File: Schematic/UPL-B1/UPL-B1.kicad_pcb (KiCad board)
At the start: 2 copper layers, 154.7 x 128.7 mm, 0 parts

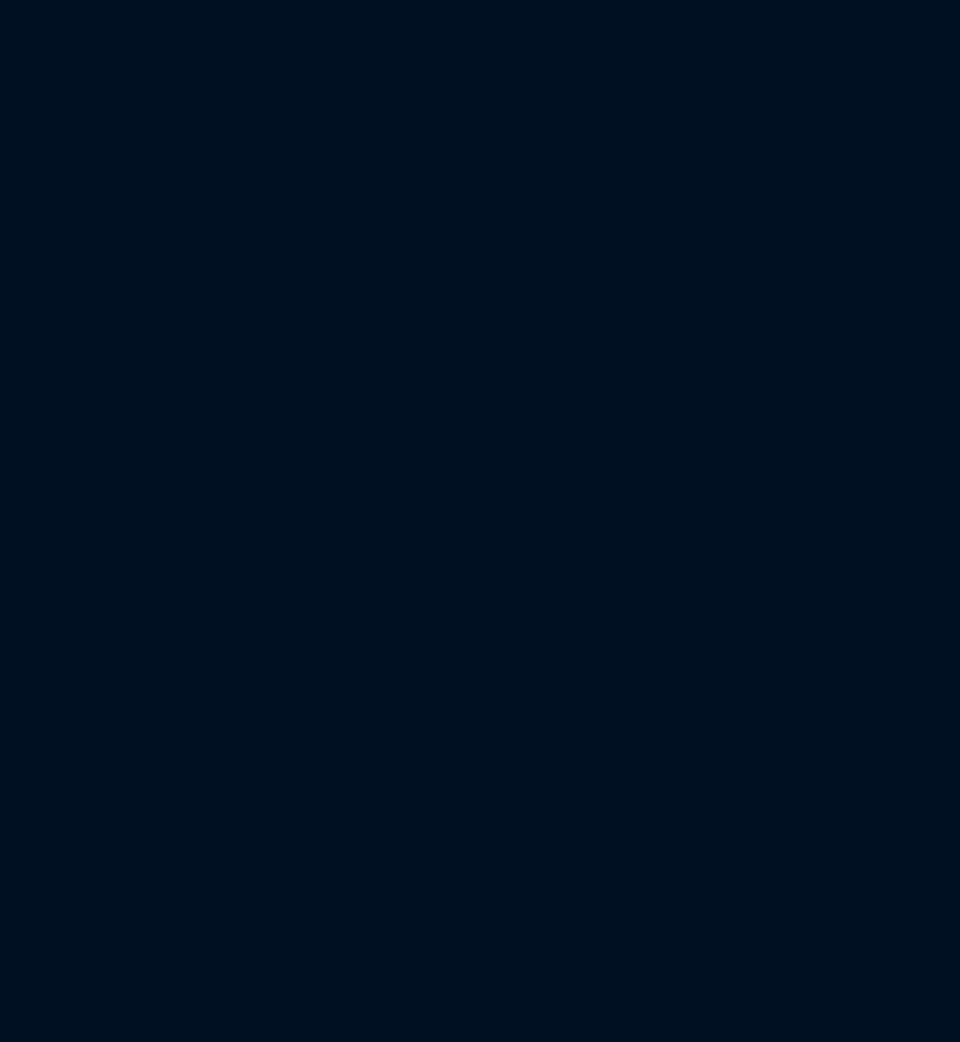
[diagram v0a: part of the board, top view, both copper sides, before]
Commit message: Minor fixups for layout.
Reannotate, deduplicate N53B. Add some hierachical pins. First
preparations for layout
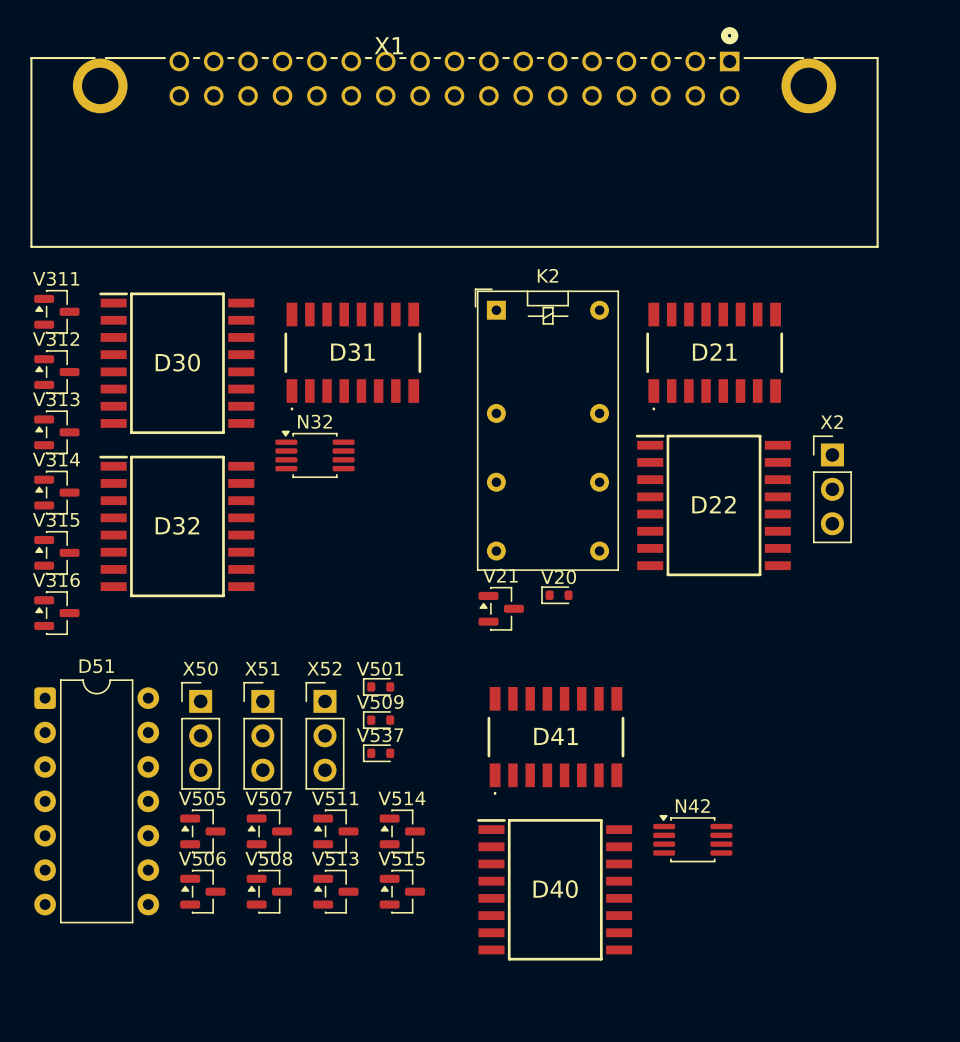
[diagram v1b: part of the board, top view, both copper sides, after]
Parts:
- added D21: 74HCT4094D,118, UPL_B1:74HCT4094D118, F.Cu at (25.4, 45.4)
- added D22: DAC8143FSZ, UPL_B1:SOIC127P1032X265-16N, F.Cu at (25.4, 56.6)
- added D30: DAC8143FSZ, UPL_B1:SOIC127P1032X265-16N, F.Cu at (-14.3, 46.1)
- added D31: 74HCT4094D,118, UPL_B1:74HCT4094D118, F.Cu at (-1.31, 45.4)
- added D32: DAC8143FSZ, UPL_B1:SOIC127P1032X265-16N, F.Cu at (-14.3, 58.2)
- added D40: DAC8143FSZ, UPL_B1:SOIC127P1032X265-16N, F.Cu at (13.6, 85.0)
- added D41: 74HCT4094D,118, UPL_B1:74HCT4094D118, F.Cu at (13.7, 73.7)
- added D51: MC1595, Package_DIP:DIP-14_W7.62mm, F.Cu at (-24.0, 70.9)
- added K2: G5V-2_Split, Relay_THT:Relay_DPDT_Omron_G5V-2, F.Cu at (9.29, 42.2)
- added N32: HA7-5221, Package_SO:MSOP-8_3x3mm_P0.65mm, F.Cu at (-4.10, 52.9)
- added N42: HA7-5221, Package_SO:MSOP-8_3x3mm_P0.65mm, F.Cu at (23.8, 81.3)
- added V20: BAS32, Diode_SMD:D_SOD-523, F.Cu at (13.9, 63.3)
- added V21: BC850B, Package_TO_SOT_SMD:SOT-23, F.Cu at (9.65, 64.3)
- added V311: BAV70, Package_TO_SOT_SMD:SOT-23, F.Cu at (-23.2, 42.3)
- added V312: BAV70, Package_TO_SOT_SMD:SOT-23, F.Cu at (-23.2, 46.8)
- added V313: BAV70, Package_TO_SOT_SMD:SOT-23, F.Cu at (-23.2, 51.2)
- added V314: BAV99, Package_TO_SOT_SMD:SOT-23, F.Cu at (-23.2, 55.7)
- added V315: BC860, Package_TO_SOT_SMD:SOT-23, F.Cu at (-23.2, 60.1)
- added V316: BC860, Package_TO_SOT_SMD:SOT-23, F.Cu at (-23.2, 64.6)
- added V501: BAS32, Diode_SMD:D_SOD-523, F.Cu at (0.75, 70.0)
- added V505: BC850B, Package_TO_SOT_SMD:SOT-23, F.Cu at (-12.4, 80.7)
- added V506: BC850B, Package_TO_SOT_SMD:SOT-23, F.Cu at (-12.4, 85.2)
- added V507: BC860B, Package_TO_SOT_SMD:SOT-23, F.Cu at (-7.47, 80.7)
- added V508: BC860B, Package_TO_SOT_SMD:SOT-23, F.Cu at (-7.47, 85.2)
- added V509: BAS32, Diode_SMD:D_SOD-523, F.Cu at (0.75, 72.5)
- added V511: BAV70, Package_TO_SOT_SMD:SOT-23, F.Cu at (-2.56, 80.7)
- added V513: BAV99, Package_TO_SOT_SMD:SOT-23, F.Cu at (-2.56, 85.2)
- added V514: BAV99, Package_TO_SOT_SMD:SOT-23, F.Cu at (2.35, 80.7)
- added V515: BAV99, Package_TO_SOT_SMD:SOT-23, F.Cu at (2.35, 85.2)
- added V537: BAS32, Diode_SMD:D_SOD-523, F.Cu at (0.75, 74.9)
- added X1: 5102159-8, UPL_B1:TYCO_5102159-8, F.Cu at (-14.1, 26.4)
- added X2: Conn_01x03_Pin_Bridge, Connector_PinHeader_2.54mm:PinHeader_1x03_P2.54mm_Vertical, F.Cu at (34.1, 52.9)
- added X50: Conn_01x03_Pin_Bridge, Connector_PinHeader_2.54mm:PinHeader_1x03_P2.54mm_Vertical, F.Cu at (-12.5, 71.1)
- added X51: Conn_01x03_Pin_Bridge, Connector_PinHeader_2.54mm:PinHeader_1x03_P2.54mm_Vertical, F.Cu at (-7.95, 71.1)
- added X52: Conn_01x03_Pin_Bridge, Connector_PinHeader_2.54mm:PinHeader_1x03_P2.54mm_Vertical, F.Cu at (-3.36, 71.1)

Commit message: updated DXF files for PCB
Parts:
- moved X1 123.3 mm to (36.6, 138.7)
- moved D21 45.9 mm to (-20.5, 46.8)
- moved D22 45.9 mm to (-20.5, 58.0)
- moved D30 45.9 mm to (-60.2, 47.5)
- moved D31 45.9 mm to (-47.2, 46.8)
- moved D32 45.9 mm to (-60.2, 59.6)
- moved D40 45.9 mm to (-32.3, 86.4)
- moved D41 45.9 mm to (-32.2, 75.1)
- moved K2 45.9 mm to (-36.6, 43.6)
- moved N32 45.9 mm to (-50.0, 54.3)
- moved N42 45.9 mm to (-22.1, 82.7)
- moved V20 45.9 mm to (-32.0, 64.7)
- moved V21 45.9 mm to (-36.3, 65.7)
- moved V311 45.9 mm to (-69.1, 43.7)
- moved V312 45.9 mm to (-69.1, 48.2)
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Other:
- board size 154.7 x 128.7 mm -> 155 x 130 mm
- board text added: "Origin for Graphics Import X180,Y20 Rotate if needed to have notch at bottom"

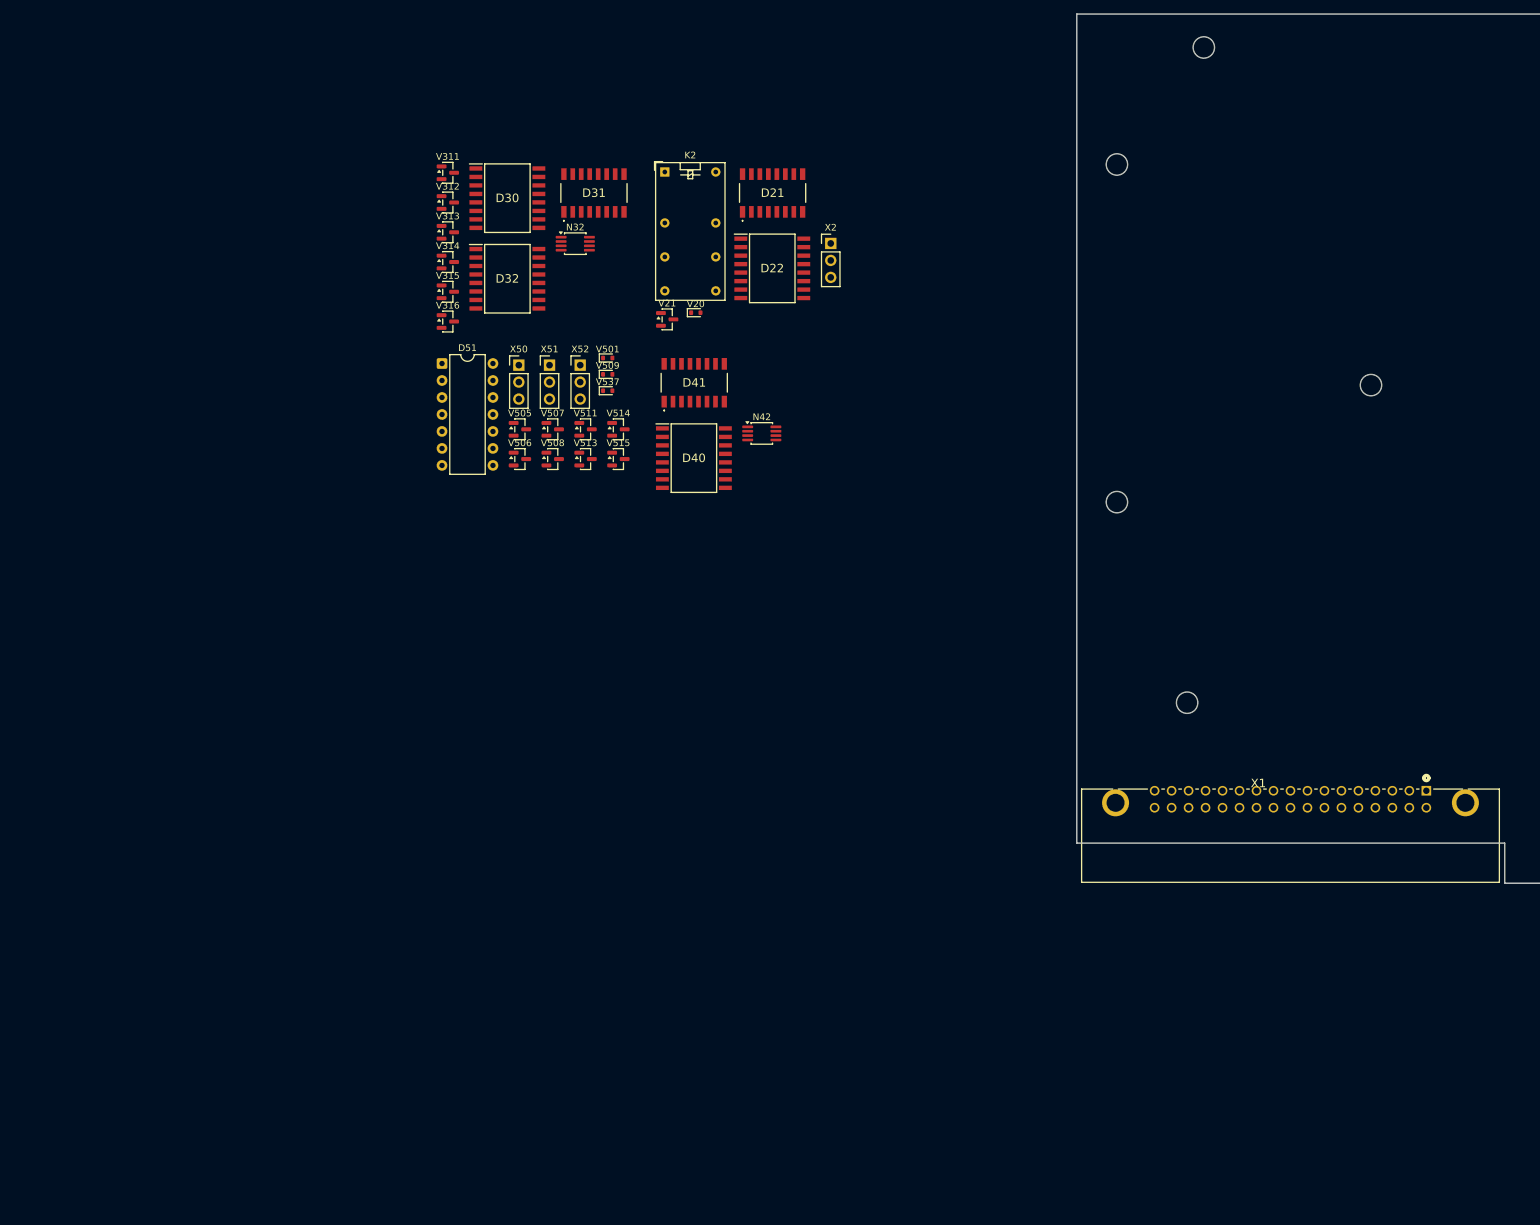
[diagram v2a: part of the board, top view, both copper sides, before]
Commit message: added majority of footprints
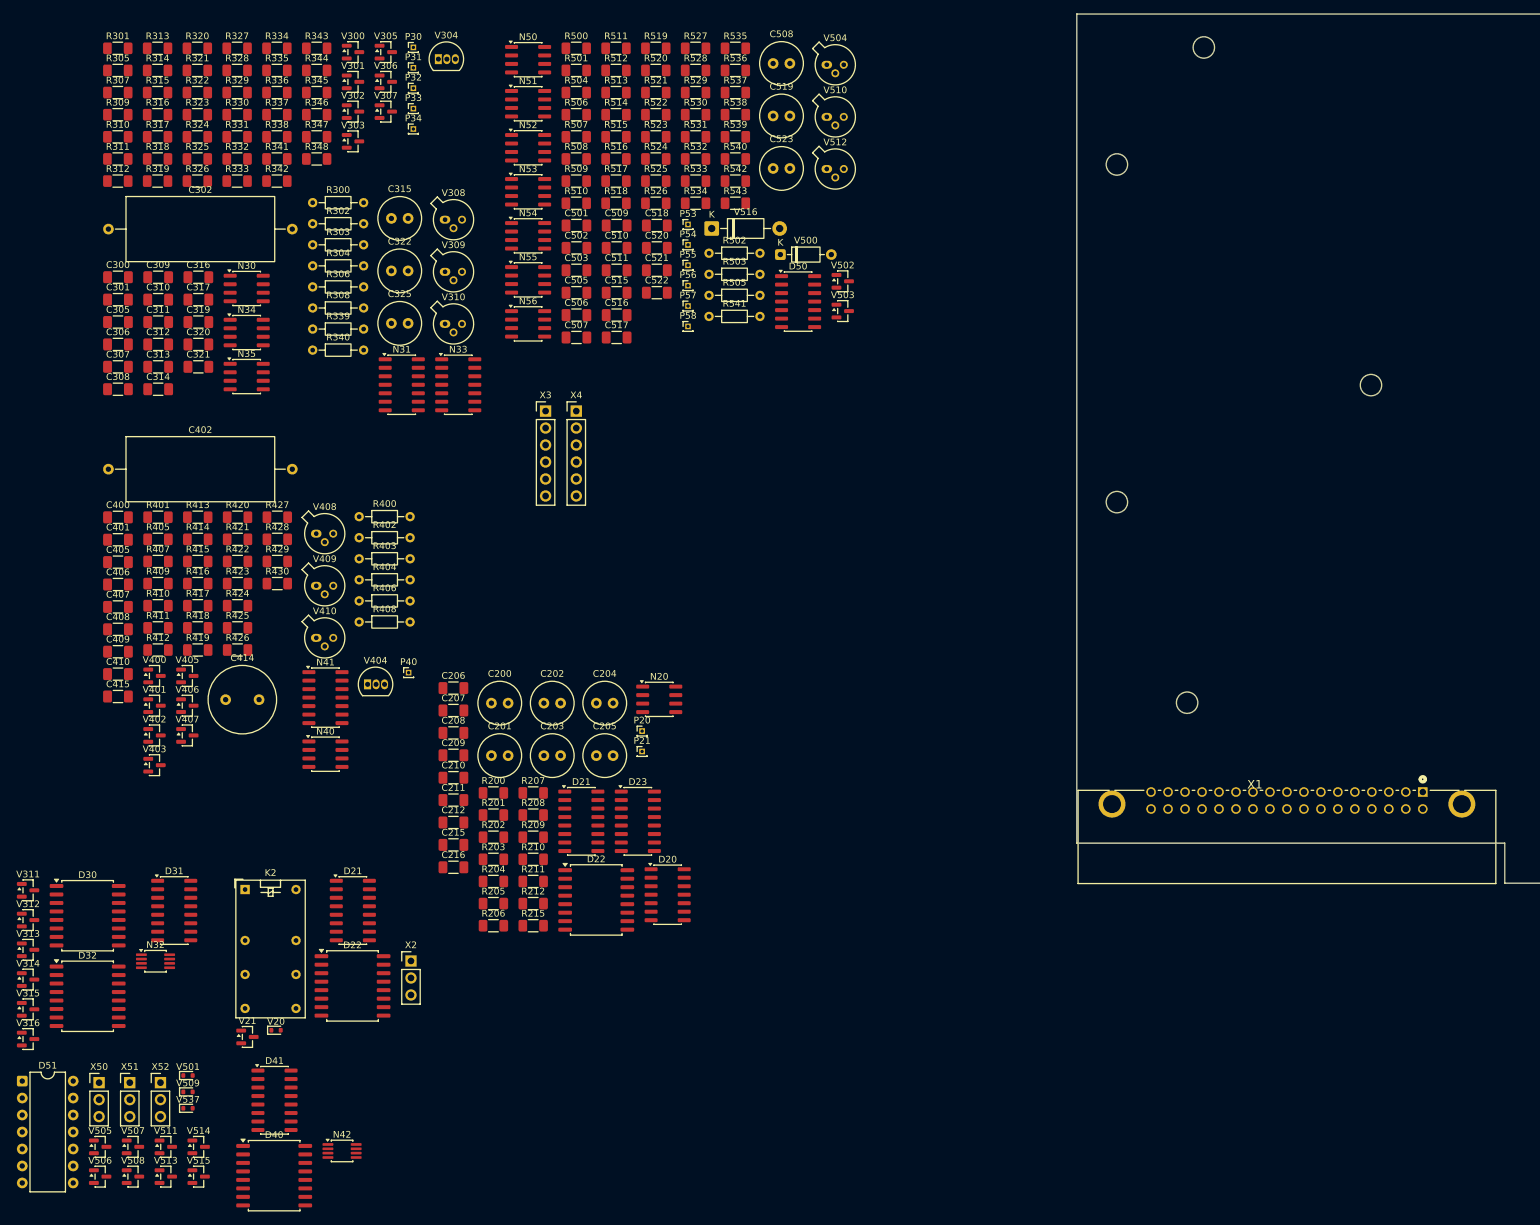
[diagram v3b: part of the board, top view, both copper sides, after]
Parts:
- added C200: 100uF 25V, Capacitor_THT:C_Radial_D6.3mm_H11.0mm_P2.50mm, F.Cu at (-62.6, 123.1)
- added C201: 100uF 25V, Capacitor_THT:C_Radial_D6.3mm_H11.0mm_P2.50mm, F.Cu at (-62.6, 130.9)
- added C202: 100uF 25V, Capacitor_THT:C_Radial_D6.3mm_H11.0mm_P2.50mm, F.Cu at (-54.7, 123.1)
- added C203: 100uF 25V, Capacitor_THT:C_Radial_D6.3mm_H11.0mm_P2.50mm, F.Cu at (-54.7, 130.9)
- added C204: 100uF 25V, Capacitor_THT:C_Radial_D6.3mm_H11.0mm_P2.50mm, F.Cu at (-46.9, 123.1)
- added C205: 100uF 25V, Capacitor_THT:C_Radial_D6.3mm_H11.0mm_P2.50mm, F.Cu at (-46.9, 130.9)
- added C206: 100nF, Capacitor_SMD:C_1206_3216Metric_Pad1.33x1.80mm_HandSolder, F.Cu at (-68.2, 120.8)
- added C207: 100nF, Capacitor_SMD:C_1206_3216Metric_Pad1.33x1.80mm_HandSolder, F.Cu at (-68.2, 124.2)
- added C208: 100nF, Capacitor_SMD:C_1206_3216Metric_Pad1.33x1.80mm_HandSolder, F.Cu at (-68.2, 127.5)
- added C209: 100nF, Capacitor_SMD:C_1206_3216Metric_Pad1.33x1.80mm_HandSolder, F.Cu at (-68.2, 130.9)
- added C210: 100nF, Capacitor_SMD:C_1206_3216Metric_Pad1.33x1.80mm_HandSolder, F.Cu at (-68.2, 134.2)
- added C211: 100nF, Capacitor_SMD:C_1206_3216Metric_Pad1.33x1.80mm_HandSolder, F.Cu at (-68.2, 137.6)
- added C212: 100nF, Capacitor_SMD:C_1206_3216Metric_Pad1.33x1.80mm_HandSolder, F.Cu at (-68.2, 140.9)
- added C215: 3p9F, Capacitor_SMD:C_1206_3216Metric_Pad1.33x1.80mm_HandSolder, F.Cu at (-68.2, 144.3)
- added C216: 3p9F, Capacitor_SMD:C_1206_3216Metric_Pad1.33x1.80mm_HandSolder, F.Cu at (-68.2, 147.6)
- added C300: 3p9F, Capacitor_SMD:C_1206_3216Metric_Pad1.33x1.80mm_HandSolder, F.Cu at (-118.4, 59.4)
- added C301: 3p9F, Capacitor_SMD:C_1206_3216Metric_Pad1.33x1.80mm_HandSolder, F.Cu at (-118.4, 62.7)
- added C302: 330nF, Capacitor_THT:C_Axial_L22.0mm_D9.5mm_P27.50mm_Horizontal, F.Cu at (-119.8, 52.2)
- added C305: 560pF, Capacitor_SMD:C_1206_3216Metric_Pad1.33x1.80mm_HandSolder, F.Cu at (-118.4, 66.1)
- added C306: 100nF, Capacitor_SMD:C_1206_3216Metric_Pad1.33x1.80mm_HandSolder, F.Cu at (-118.4, 69.4)
- added C307: 100nF, Capacitor_SMD:C_1206_3216Metric_Pad1.33x1.80mm_HandSolder, F.Cu at (-118.4, 72.8)
- added C308: 100nF, Capacitor_SMD:C_1206_3216Metric_Pad1.33x1.80mm_HandSolder, F.Cu at (-118.4, 76.1)
- added C309: 3p9F, Capacitor_SMD:C_1206_3216Metric_Pad1.33x1.80mm_HandSolder, F.Cu at (-112.4, 59.4)
- added C310: 3p9F, Capacitor_SMD:C_1206_3216Metric_Pad1.33x1.80mm_HandSolder, F.Cu at (-112.4, 62.7)
- added C311: 3p9F, Capacitor_SMD:C_1206_3216Metric_Pad1.33x1.80mm_HandSolder, F.Cu at (-112.4, 66.1)
- added C312: 3p9F, Capacitor_SMD:C_1206_3216Metric_Pad1.33x1.80mm_HandSolder, F.Cu at (-112.4, 69.4)
- added C313: 100nF, Capacitor_SMD:C_1206_3216Metric_Pad1.33x1.80mm_HandSolder, F.Cu at (-112.4, 72.8)
- added C314: 100nF, Capacitor_SMD:C_1206_3216Metric_Pad1.33x1.80mm_HandSolder, F.Cu at (-112.4, 76.1)
- added C315: 47uF 50V, Capacitor_THT:C_Radial_D6.3mm_H11.0mm_P2.50mm, F.Cu at (-77.5, 50.6)
- added C316: 100nF, Capacitor_SMD:C_1206_3216Metric_Pad1.33x1.80mm_HandSolder, F.Cu at (-106.4, 59.4)
- added C317: 100nF, Capacitor_SMD:C_1206_3216Metric_Pad1.33x1.80mm_HandSolder, F.Cu at (-106.4, 62.7)
- added C319: 3p3F, Capacitor_SMD:C_1206_3216Metric_Pad1.33x1.80mm_HandSolder, F.Cu at (-106.4, 66.1)
- added C320: 330pF, Capacitor_SMD:C_1206_3216Metric_Pad1.33x1.80mm_HandSolder, F.Cu at (-106.4, 69.4)
- added C321: 330pF, Capacitor_SMD:C_1206_3216Metric_Pad1.33x1.80mm_HandSolder, F.Cu at (-106.4, 72.8)
- added C322: 100uF 25V, Capacitor_THT:C_Radial_D6.3mm_H11.0mm_P2.50mm, F.Cu at (-77.5, 58.4)
- added C325: 100uF 25V, Capacitor_THT:C_Radial_D6.3mm_H11.0mm_P2.50mm, F.Cu at (-77.5, 66.3)
- added C400: 3p9F, Capacitor_SMD:C_1206_3216Metric_Pad1.33x1.80mm_HandSolder, F.Cu at (-118.4, 95.3)
- added C401: 3p9F, Capacitor_SMD:C_1206_3216Metric_Pad1.33x1.80mm_HandSolder, F.Cu at (-118.4, 98.6)
- added C402: 330nF, Capacitor_THT:C_Axial_L22.0mm_D9.5mm_P27.50mm_Horizontal, F.Cu at (-119.8, 88.1)
- added C405: 560pF, Capacitor_SMD:C_1206_3216Metric_Pad1.33x1.80mm_HandSolder, F.Cu at (-118.4, 102.0)
- added C406: 100nF, Capacitor_SMD:C_1206_3216Metric_Pad1.33x1.80mm_HandSolder, F.Cu at (-118.4, 105.3)
- added C407: 100nF, Capacitor_SMD:C_1206_3216Metric_Pad1.33x1.80mm_HandSolder, F.Cu at (-118.4, 108.7)
- added C408: 100nF, Capacitor_SMD:C_1206_3216Metric_Pad1.33x1.80mm_HandSolder, F.Cu at (-118.4, 112.0)
- added C409: 100nF, Capacitor_SMD:C_1206_3216Metric_Pad1.33x1.80mm_HandSolder, F.Cu at (-118.4, 115.4)
- added C410: 100nF, Capacitor_SMD:C_1206_3216Metric_Pad1.33x1.80mm_HandSolder, F.Cu at (-118.4, 118.7)
- added C414: 220uF 35V, Capacitor_THT:C_Radial_D10.0mm_H12.5mm_P5.00mm, F.Cu at (-102.3, 122.5)
- added C415: 330pF, Capacitor_SMD:C_1206_3216Metric_Pad1.33x1.80mm_HandSolder, F.Cu at (-118.4, 122.1)
- added C501: 15pF, Capacitor_SMD:C_1206_3216Metric_Pad1.33x1.80mm_HandSolder, F.Cu at (-49.8, 51.6)
- added C502: 33pF, Capacitor_SMD:C_1206_3216Metric_Pad1.33x1.80mm_HandSolder, F.Cu at (-49.8, 55.0)
- added C503: 4p7F, Capacitor_SMD:C_1206_3216Metric_Pad1.33x1.80mm_HandSolder, F.Cu at (-49.8, 58.3)
- added C505: 33pF, Capacitor_SMD:C_1206_3216Metric_Pad1.33x1.80mm_HandSolder, F.Cu at (-49.8, 61.7)
- added C506: 100nF, Capacitor_SMD:C_1206_3216Metric_Pad1.33x1.80mm_HandSolder, F.Cu at (-49.8, 65.0)
- added C507: 100nF, Capacitor_SMD:C_1206_3216Metric_Pad1.33x1.80mm_HandSolder, F.Cu at (-49.8, 68.4)
- added C508: 10uF 50V, Capacitor_THT:C_Radial_D6.3mm_H11.0mm_P2.50mm, F.Cu at (-20.4, 27.4)
- added C509: 3n3F, Capacitor_SMD:C_1206_3216Metric_Pad1.33x1.80mm_HandSolder, F.Cu at (-43.8, 51.6)
- added C510: 15pF, Capacitor_SMD:C_1206_3216Metric_Pad1.33x1.80mm_HandSolder, F.Cu at (-43.8, 55.0)
- added C511: 100nF, Capacitor_SMD:C_1206_3216Metric_Pad1.33x1.80mm_HandSolder, F.Cu at (-43.8, 58.3)
- added C515: 100nF, Capacitor_SMD:C_1206_3216Metric_Pad1.33x1.80mm_HandSolder, F.Cu at (-43.8, 61.7)
- added C516: 100nF, Capacitor_SMD:C_1206_3216Metric_Pad1.33x1.80mm_HandSolder, F.Cu at (-43.8, 65.0)
- added C517: 100nF, Capacitor_SMD:C_1206_3216Metric_Pad1.33x1.80mm_HandSolder, F.Cu at (-43.8, 68.4)
- added C518: 100nF, Capacitor_SMD:C_1206_3216Metric_Pad1.33x1.80mm_HandSolder, F.Cu at (-37.8, 51.6)
- added C519: 100uF 25V, Capacitor_THT:C_Radial_D6.3mm_H11.0mm_P2.50mm, F.Cu at (-20.4, 35.2)
- added C520: 27pF, Capacitor_SMD:C_1206_3216Metric_Pad1.33x1.80mm_HandSolder, F.Cu at (-37.8, 55.0)
- added C521: 8p2F, Capacitor_SMD:C_1206_3216Metric_Pad1.33x1.80mm_HandSolder, F.Cu at (-37.8, 58.3)
- added C522: 1pF, Capacitor_SMD:C_1206_3216Metric_Pad1.33x1.80mm_HandSolder, F.Cu at (-37.8, 61.7)
- added C523: 2u2F 50V, Capacitor_THT:C_Radial_D6.3mm_H11.0mm_P2.50mm, F.Cu at (-20.4, 43.1)
- added D20: 74HC86, Package_SO:SOIC-14_3.9x8.7mm_P1.27mm, F.Cu at (-36.2, 151.7)
- added D21: 74HCT4094T-L, Package_SO:SOIC-16_3.9x9.9mm_P1.27mm, F.Cu at (-49.1, 140.7)
- added D22: DAC8143FSZ, Package_SO:SOIC-16W_7.5x10.3mm_P1.27mm, F.Cu at (-46.9, 152.5)
- added D23: 74HC165, Package_SO:SOIC-16_3.9x9.9mm_P1.27mm, F.Cu at (-40.7, 140.7)
- added D50: 74HC132T, Package_SO:SOIC-14_3.9x8.7mm_P1.27mm, F.Cu at (-16.7, 63.0)
- added N20: NE5534 / SE5534, Package_SO:SOIC-8_3.9x4.9mm_P1.27mm, F.Cu at (-37.5, 122.5)
- added N30: NE5534 / SE5534, Package_SO:SOIC-8_3.9x4.9mm_P1.27mm, F.Cu at (-99.2, 61.0)
- added N31: LM339, Package_SO:SOIC-14_3.9x8.7mm_P1.27mm, F.Cu at (-76.0, 75.5)
- added N33: LM339, Package_SO:SOIC-14_3.9x8.7mm_P1.27mm, F.Cu at (-67.5, 75.5)
- added N34: NE5534 / SE5534, Package_SO:SOIC-8_3.9x4.9mm_P1.27mm, F.Cu at (-99.2, 67.6)
- added N35: NE5534 / SE5534, Package_SO:SOIC-8_3.9x4.9mm_P1.27mm, F.Cu at (-99.2, 74.2)
- added N40: NE5534 / SE5534, Package_SO:SOIC-8_3.9x4.9mm_P1.27mm, F.Cu at (-87.4, 130.7)
- added N41: LM339, Package_SO:SOIC-14_3.9x8.7mm_P1.27mm, F.Cu at (-87.4, 122.2)
- added N50: LM2903, Package_SO:SOIC-8_3.9x4.9mm_P1.27mm, F.Cu at (-57.1, 26.8)
- added N51: NE5534 / SE5534, Package_SO:SOIC-8_3.9x4.9mm_P1.27mm, F.Cu at (-57.1, 33.4)
- added N52: LM211, Package_SO:SOIC-8_3.9x4.9mm_P1.27mm, F.Cu at (-57.1, 40.0)
- added N53: TL072, Package_SO:SOIC-8_3.9x4.9mm_P1.27mm, F.Cu at (-57.1, 46.6)
- added N54: TL072, Package_SO:SOIC-8_3.9x4.9mm_P1.27mm, F.Cu at (-57.1, 53.2)
- added N55: TL072, Package_SO:SOIC-8_3.9x4.9mm_P1.27mm, F.Cu at (-57.1, 59.8)
- added N56: TL072, Package_SO:SOIC-8_3.9x4.9mm_P1.27mm, F.Cu at (-57.1, 66.3)
- added P20: TestPoint, Connector_PinHeader_1.00mm:PinHeader_1x01_P1.00mm_Vertical, F.Cu at (-40.0, 127.2)
- added P21: TestPoint, Connector_PinHeader_1.00mm:PinHeader_1x01_P1.00mm_Vertical, F.Cu at (-40.0, 130.3)
- added P30: TestPoint, Connector_PinHeader_1.00mm:PinHeader_1x01_P1.00mm_Vertical, F.Cu at (-74.2, 25.0)
- added P31: TestPoint, Connector_PinHeader_1.00mm:PinHeader_1x01_P1.00mm_Vertical, F.Cu at (-74.2, 28.0)
- added P32: TestPoint, Connector_PinHeader_1.00mm:PinHeader_1x01_P1.00mm_Vertical, F.Cu at (-74.2, 31.1)
- added P33: TestPoint, Connector_PinHeader_1.00mm:PinHeader_1x01_P1.00mm_Vertical, F.Cu at (-74.2, 34.1)
- added P34: TestPoint, Connector_PinHeader_1.00mm:PinHeader_1x01_P1.00mm_Vertical, F.Cu at (-74.2, 37.2)
- added P40: TestPoint, Connector_PinHeader_1.00mm:PinHeader_1x01_P1.00mm_Vertical, F.Cu at (-74.9, 118.5)
- added P53: TestPoint, Connector_PinHeader_1.00mm:PinHeader_1x01_P1.00mm_Vertical, F.Cu at (-33.1, 51.5)
- added P54: TestPoint, Connector_PinHeader_1.00mm:PinHeader_1x01_P1.00mm_Vertical, F.Cu at (-33.1, 54.5)
- added P55: TestPoint, Connector_PinHeader_1.00mm:PinHeader_1x01_P1.00mm_Vertical, F.Cu at (-33.1, 57.6)
- added P56: TestPoint, Connector_PinHeader_1.00mm:PinHeader_1x01_P1.00mm_Vertical, F.Cu at (-33.1, 60.6)
- added P57: TestPoint, Connector_PinHeader_1.00mm:PinHeader_1x01_P1.00mm_Vertical, F.Cu at (-33.1, 63.7)
- added P58: TestPoint, Connector_PinHeader_1.00mm:PinHeader_1x01_P1.00mm_Vertical, F.Cu at (-33.1, 66.7)
- added R200: 10K, Resistor_SMD:R_1206_3216Metric_Pad1.30x1.75mm_HandSolder, F.Cu at (-62.3, 136.5)
- added R201: 10K, Resistor_SMD:R_1206_3216Metric_Pad1.30x1.75mm_HandSolder, F.Cu at (-62.3, 139.8)
- added R202: 10K, Resistor_SMD:R_1206_3216Metric_Pad1.30x1.75mm_HandSolder, F.Cu at (-62.3, 143.1)
- added R203: 10, Resistor_SMD:R_1206_3216Metric_Pad1.30x1.75mm_HandSolder, F.Cu at (-62.3, 146.4)
- added R204: 10, Resistor_SMD:R_1206_3216Metric_Pad1.30x1.75mm_HandSolder, F.Cu at (-62.3, 149.7)
- added R205: 10, Resistor_SMD:R_1206_3216Metric_Pad1.30x1.75mm_HandSolder, F.Cu at (-62.3, 153.0)
- added R206: 1K, Resistor_SMD:R_1206_3216Metric_Pad1.30x1.75mm_HandSolder, F.Cu at (-62.3, 156.4)
- added R207: 1K, Resistor_SMD:R_1206_3216Metric_Pad1.30x1.75mm_HandSolder, F.Cu at (-56.3, 136.5)
- added R208: 1K, Resistor_SMD:R_1206_3216Metric_Pad1.30x1.75mm_HandSolder, F.Cu at (-56.3, 139.8)
- added R209: 1K, Resistor_SMD:R_1206_3216Metric_Pad1.30x1.75mm_HandSolder, F.Cu at (-56.3, 143.1)
- added R210: 1K, Resistor_SMD:R_1206_3216Metric_Pad1.30x1.75mm_HandSolder, F.Cu at (-56.3, 146.4)
- added R211: 1K, Resistor_SMD:R_1206_3216Metric_Pad1.30x1.75mm_HandSolder, F.Cu at (-56.3, 149.7)
- added R212: 1K, Resistor_SMD:R_1206_3216Metric_Pad1.30x1.75mm_HandSolder, F.Cu at (-56.3, 153.0)
- added R215: 47R5, Resistor_SMD:R_1206_3216Metric_Pad1.30x1.75mm_HandSolder, F.Cu at (-56.3, 156.4)
- added R300: 5K05 0.1%, Resistor_THT:R_Axial_DIN0204_L3.6mm_D1.6mm_P7.62mm_Horizontal, F.Cu at (-89.3, 48.2)
- added R301: 511K, Resistor_SMD:R_1206_3216Metric_Pad1.30x1.75mm_HandSolder, F.Cu at (-118.4, 25.1)
- added R302: 10K 0.1%, Resistor_THT:R_Axial_DIN0204_L3.6mm_D1.6mm_P7.62mm_Horizontal, F.Cu at (-89.3, 51.4)
- added R303: 20K 0.1%, Resistor_THT:R_Axial_DIN0204_L3.6mm_D1.6mm_P7.62mm_Horizontal, F.Cu at (-89.3, 54.5)
- added R304: 38K8 0.1%, Resistor_THT:R_Axial_DIN0204_L3.6mm_D1.6mm_P7.62mm_Horizontal, F.Cu at (-89.3, 57.7)
- added R305: 1K21, Resistor_SMD:R_1206_3216Metric_Pad1.30x1.75mm_HandSolder, F.Cu at (-118.4, 28.4)
- added R306: 41K7 0.1%, Resistor_THT:R_Axial_DIN0204_L3.6mm_D1.6mm_P7.62mm_Horizontal, F.Cu at (-89.3, 60.8)
- added R307: 1M, Resistor_SMD:R_1206_3216Metric_Pad1.30x1.75mm_HandSolder, F.Cu at (-118.4, 31.7)
- added R308: 41K7 0.1%, Resistor_THT:R_Axial_DIN0204_L3.6mm_D1.6mm_P7.62mm_Horizontal, F.Cu at (-89.3, 64.0)
- added R309: 1M, Resistor_SMD:R_1206_3216Metric_Pad1.30x1.75mm_HandSolder, F.Cu at (-118.4, 35.1)
- added R310: 1K, Resistor_SMD:R_1206_3216Metric_Pad1.30x1.75mm_HandSolder, F.Cu at (-118.4, 38.4)
- added R311: 1K, Resistor_SMD:R_1206_3216Metric_Pad1.30x1.75mm_HandSolder, F.Cu at (-118.4, 41.7)
- added R312: 15K, Resistor_SMD:R_1206_3216Metric_Pad1.30x1.75mm_HandSolder, F.Cu at (-118.4, 45.0)
- added R313: 15K, Resistor_SMD:R_1206_3216Metric_Pad1.30x1.75mm_HandSolder, F.Cu at (-112.5, 25.1)
- added R314: 15K, Resistor_SMD:R_1206_3216Metric_Pad1.30x1.75mm_HandSolder, F.Cu at (-112.5, 28.4)
- added R315: 15K, Resistor_SMD:R_1206_3216Metric_Pad1.30x1.75mm_HandSolder, F.Cu at (-112.5, 31.7)
- added R316: 15K, Resistor_SMD:R_1206_3216Metric_Pad1.30x1.75mm_HandSolder, F.Cu at (-112.5, 35.1)
- added R317: 15K, Resistor_SMD:R_1206_3216Metric_Pad1.30x1.75mm_HandSolder, F.Cu at (-112.5, 38.4)
- added R318: 15K, Resistor_SMD:R_1206_3216Metric_Pad1.30x1.75mm_HandSolder, F.Cu at (-112.5, 41.7)
- added R319: 15K, Resistor_SMD:R_1206_3216Metric_Pad1.30x1.75mm_HandSolder, F.Cu at (-112.5, 45.0)
- added R320: 1K, Resistor_SMD:R_1206_3216Metric_Pad1.30x1.75mm_HandSolder, F.Cu at (-106.5, 25.1)
- added R321: 100K, Resistor_SMD:R_1206_3216Metric_Pad1.30x1.75mm_HandSolder, F.Cu at (-106.5, 28.4)
- added R322: 100K, Resistor_SMD:R_1206_3216Metric_Pad1.30x1.75mm_HandSolder, F.Cu at (-106.5, 31.7)
- added R323: 100K, Resistor_SMD:R_1206_3216Metric_Pad1.30x1.75mm_HandSolder, F.Cu at (-106.5, 35.1)
- added R324: 100K, Resistor_SMD:R_1206_3216Metric_Pad1.30x1.75mm_HandSolder, F.Cu at (-106.5, 38.4)
- added R325: 100K, Resistor_SMD:R_1206_3216Metric_Pad1.30x1.75mm_HandSolder, F.Cu at (-106.5, 41.7)
- added R326: 100K, Resistor_SMD:R_1206_3216Metric_Pad1.30x1.75mm_HandSolder, F.Cu at (-106.5, 45.0)
- added R327: 10K, Resistor_SMD:R_1206_3216Metric_Pad1.30x1.75mm_HandSolder, F.Cu at (-100.6, 25.1)
- added R328: 10K, Resistor_SMD:R_1206_3216Metric_Pad1.30x1.75mm_HandSolder, F.Cu at (-100.6, 28.4)
- added R329: 10K, Resistor_SMD:R_1206_3216Metric_Pad1.30x1.75mm_HandSolder, F.Cu at (-100.6, 31.7)
- added R330: 15K, Resistor_SMD:R_1206_3216Metric_Pad1.30x1.75mm_HandSolder, F.Cu at (-100.6, 35.1)
- added R331: 15K, Resistor_SMD:R_1206_3216Metric_Pad1.30x1.75mm_HandSolder, F.Cu at (-100.6, 38.4)
- added R332: 15K, Resistor_SMD:R_1206_3216Metric_Pad1.30x1.75mm_HandSolder, F.Cu at (-100.6, 41.7)
- added R333: 7K5, Resistor_SMD:R_1206_3216Metric_Pad1.30x1.75mm_HandSolder, F.Cu at (-100.6, 45.0)
- added R334: 7K5, Resistor_SMD:R_1206_3216Metric_Pad1.30x1.75mm_HandSolder, F.Cu at (-94.6, 25.1)
- added R335: 100K, Resistor_SMD:R_1206_3216Metric_Pad1.30x1.75mm_HandSolder, F.Cu at (-94.6, 28.4)
- added R336: 100K, Resistor_SMD:R_1206_3216Metric_Pad1.30x1.75mm_HandSolder, F.Cu at (-94.6, 31.7)
- added R337: 3K32, Resistor_SMD:R_1206_3216Metric_Pad1.30x1.75mm_HandSolder, F.Cu at (-94.6, 35.1)
- added R338: 3K32, Resistor_SMD:R_1206_3216Metric_Pad1.30x1.75mm_HandSolder, F.Cu at (-94.6, 38.4)
- added R339: 4K75 0.1%, Resistor_THT:R_Axial_DIN0204_L3.6mm_D1.6mm_P7.62mm_Horizontal, F.Cu at (-89.3, 67.1)
- added R340: 4K75 0.1%, Resistor_THT:R_Axial_DIN0204_L3.6mm_D1.6mm_P7.62mm_Horizontal, F.Cu at (-89.3, 70.3)
- added R341: 1K, Resistor_SMD:R_1206_3216Metric_Pad1.30x1.75mm_HandSolder, F.Cu at (-94.6, 41.7)
- added R342: 1K, Resistor_SMD:R_1206_3216Metric_Pad1.30x1.75mm_HandSolder, F.Cu at (-94.6, 45.0)
- added R343: 121K, Resistor_SMD:R_1206_3216Metric_Pad1.30x1.75mm_HandSolder, F.Cu at (-88.7, 25.1)
- added R344: 100, Resistor_SMD:R_1206_3216Metric_Pad1.30x1.75mm_HandSolder, F.Cu at (-88.7, 28.4)
- added R345: 47K5, Resistor_SMD:R_1206_3216Metric_Pad1.30x1.75mm_HandSolder, F.Cu at (-88.7, 31.7)
- added R346: 100, Resistor_SMD:R_1206_3216Metric_Pad1.30x1.75mm_HandSolder, F.Cu at (-88.7, 35.1)
- added R347: 100, Resistor_SMD:R_1206_3216Metric_Pad1.30x1.75mm_HandSolder, F.Cu at (-88.7, 38.4)
- added R348: 100, Resistor_SMD:R_1206_3216Metric_Pad1.30x1.75mm_HandSolder, F.Cu at (-88.7, 41.7)
- added R400: 5K05 0.1%, Resistor_THT:R_Axial_DIN0204_L3.6mm_D1.6mm_P7.62mm_Horizontal, F.Cu at (-82.3, 95.2)
- added R401: 511K, Resistor_SMD:R_1206_3216Metric_Pad1.30x1.75mm_HandSolder, F.Cu at (-112.4, 95.3)
- added R402: 10K 0.1%, Resistor_THT:R_Axial_DIN0204_L3.6mm_D1.6mm_P7.62mm_Horizontal, F.Cu at (-82.3, 98.3)
- added R403: 20K 0.1%, Resistor_THT:R_Axial_DIN0204_L3.6mm_D1.6mm_P7.62mm_Horizontal, F.Cu at (-82.3, 101.5)
- added R404: 38K8 0.1%, Resistor_THT:R_Axial_DIN0204_L3.6mm_D1.6mm_P7.62mm_Horizontal, F.Cu at (-82.3, 104.6)
- added R405: 1K21, Resistor_SMD:R_1206_3216Metric_Pad1.30x1.75mm_HandSolder, F.Cu at (-112.4, 98.6)
- added R406: 41K7 0.1%, Resistor_THT:R_Axial_DIN0204_L3.6mm_D1.6mm_P7.62mm_Horizontal, F.Cu at (-82.3, 107.8)
- added R407: 1M, Resistor_SMD:R_1206_3216Metric_Pad1.30x1.75mm_HandSolder, F.Cu at (-112.4, 101.9)
- added R408: 41K7 0.1%, Resistor_THT:R_Axial_DIN0204_L3.6mm_D1.6mm_P7.62mm_Horizontal, F.Cu at (-82.3, 110.9)
- added R409: 1M, Resistor_SMD:R_1206_3216Metric_Pad1.30x1.75mm_HandSolder, F.Cu at (-112.4, 105.2)
- added R410: 1K, Resistor_SMD:R_1206_3216Metric_Pad1.30x1.75mm_HandSolder, F.Cu at (-112.4, 108.5)
- added R411: 1K, Resistor_SMD:R_1206_3216Metric_Pad1.30x1.75mm_HandSolder, F.Cu at (-112.4, 111.8)
- added R412: 15K, Resistor_SMD:R_1206_3216Metric_Pad1.30x1.75mm_HandSolder, F.Cu at (-112.4, 115.1)
- added R413: 15K, Resistor_SMD:R_1206_3216Metric_Pad1.30x1.75mm_HandSolder, F.Cu at (-106.5, 95.3)
- added R414: 15K, Resistor_SMD:R_1206_3216Metric_Pad1.30x1.75mm_HandSolder, F.Cu at (-106.5, 98.6)
- added R415: 15K, Resistor_SMD:R_1206_3216Metric_Pad1.30x1.75mm_HandSolder, F.Cu at (-106.5, 101.9)
- added R416: 15K, Resistor_SMD:R_1206_3216Metric_Pad1.30x1.75mm_HandSolder, F.Cu at (-106.5, 105.2)
- added R417: 15K, Resistor_SMD:R_1206_3216Metric_Pad1.30x1.75mm_HandSolder, F.Cu at (-106.5, 108.5)
- added R418: 15K, Resistor_SMD:R_1206_3216Metric_Pad1.30x1.75mm_HandSolder, F.Cu at (-106.5, 111.8)
- added R419: 15K, Resistor_SMD:R_1206_3216Metric_Pad1.30x1.75mm_HandSolder, F.Cu at (-106.5, 115.1)
- added R420: 1K, Resistor_SMD:R_1206_3216Metric_Pad1.30x1.75mm_HandSolder, F.Cu at (-100.5, 95.3)
- added R421: 100K, Resistor_SMD:R_1206_3216Metric_Pad1.30x1.75mm_HandSolder, F.Cu at (-100.5, 98.6)
- added R422: 100K, Resistor_SMD:R_1206_3216Metric_Pad1.30x1.75mm_HandSolder, F.Cu at (-100.5, 101.9)
- added R423: 100K, Resistor_SMD:R_1206_3216Metric_Pad1.30x1.75mm_HandSolder, F.Cu at (-100.5, 105.2)
- added R424: 100K, Resistor_SMD:R_1206_3216Metric_Pad1.30x1.75mm_HandSolder, F.Cu at (-100.5, 108.5)
- added R425: 100K, Resistor_SMD:R_1206_3216Metric_Pad1.30x1.75mm_HandSolder, F.Cu at (-100.5, 111.8)
- added R426: 100K, Resistor_SMD:R_1206_3216Metric_Pad1.30x1.75mm_HandSolder, F.Cu at (-100.5, 115.1)
- added R427: 10K, Resistor_SMD:R_1206_3216Metric_Pad1.30x1.75mm_HandSolder, F.Cu at (-94.6, 95.3)
- added R428: 10K, Resistor_SMD:R_1206_3216Metric_Pad1.30x1.75mm_HandSolder, F.Cu at (-94.6, 98.6)
- added R429: 10K, Resistor_SMD:R_1206_3216Metric_Pad1.30x1.75mm_HandSolder, F.Cu at (-94.6, 101.9)
- added R430: 100R, Resistor_SMD:R_1206_3216Metric_Pad1.30x1.75mm_HandSolder, F.Cu at (-94.6, 105.2)
- added R500: 475, Resistor_SMD:R_1206_3216Metric_Pad1.30x1.75mm_HandSolder, F.Cu at (-49.9, 25.1)
- added R501: 475, Resistor_SMD:R_1206_3216Metric_Pad1.30x1.75mm_HandSolder, F.Cu at (-49.9, 28.4)
- added R502: 7K68, Resistor_THT:R_Axial_DIN0204_L3.6mm_D1.6mm_P7.62mm_Horizontal, F.Cu at (-30.0, 55.8)
- added R503: 4K75 0.1%, Resistor_THT:R_Axial_DIN0204_L3.6mm_D1.6mm_P7.62mm_Horizontal, F.Cu at (-30.0, 58.9)
- added R504: 20K, Resistor_SMD:R_1206_3216Metric_Pad1.30x1.75mm_HandSolder, F.Cu at (-49.9, 31.7)
- added R505: 4K75 0.1%, Resistor_THT:R_Axial_DIN0204_L3.6mm_D1.6mm_P7.62mm_Horizontal, F.Cu at (-30.0, 62.1)
- added R506: 15K, Resistor_SMD:R_1206_3216Metric_Pad1.30x1.75mm_HandSolder, F.Cu at (-49.9, 35.1)
- added R507: 15K, Resistor_SMD:R_1206_3216Metric_Pad1.30x1.75mm_HandSolder, F.Cu at (-49.9, 38.4)
- added R508: 274, Resistor_SMD:R_1206_3216Metric_Pad1.30x1.75mm_HandSolder, F.Cu at (-49.9, 41.7)
- added R509: 1K5, Resistor_SMD:R_1206_3216Metric_Pad1.30x1.75mm_HandSolder, F.Cu at (-49.9, 45.0)
- added R510: 100, Resistor_SMD:R_1206_3216Metric_Pad1.30x1.75mm_HandSolder, F.Cu at (-49.9, 48.3)
- added R511: 10K, Resistor_SMD:R_1206_3216Metric_Pad1.30x1.75mm_HandSolder, F.Cu at (-43.9, 25.1)
- added R512: 2K21, Resistor_SMD:R_1206_3216Metric_Pad1.30x1.75mm_HandSolder, F.Cu at (-43.9, 28.4)
- added R513: 10K, Resistor_SMD:R_1206_3216Metric_Pad1.30x1.75mm_HandSolder, F.Cu at (-43.9, 31.7)
- added R514: 10K, Resistor_SMD:R_1206_3216Metric_Pad1.30x1.75mm_HandSolder, F.Cu at (-43.9, 35.1)
- added R515: 10K, Resistor_SMD:R_1206_3216Metric_Pad1.30x1.75mm_HandSolder, F.Cu at (-43.9, 38.4)
- added R516: 10K, Resistor_SMD:R_1206_3216Metric_Pad1.30x1.75mm_HandSolder, F.Cu at (-43.9, 41.7)
- added R517: 100K, Resistor_SMD:R_1206_3216Metric_Pad1.30x1.75mm_HandSolder, F.Cu at (-43.9, 45.0)
- added R518: 2K21, Resistor_SMD:R_1206_3216Metric_Pad1.30x1.75mm_HandSolder, F.Cu at (-43.9, 48.3)
- added R519: 2K21, Resistor_SMD:R_1206_3216Metric_Pad1.30x1.75mm_HandSolder, F.Cu at (-38.0, 25.1)
- added R520: 2K21, Resistor_SMD:R_1206_3216Metric_Pad1.30x1.75mm_HandSolder, F.Cu at (-38.0, 28.4)
- added R521: 2K21, Resistor_SMD:R_1206_3216Metric_Pad1.30x1.75mm_HandSolder, F.Cu at (-38.0, 31.7)
- added R522: 22R1, Resistor_SMD:R_1206_3216Metric_Pad1.30x1.75mm_HandSolder, F.Cu at (-38.0, 35.1)
- added R523: 20K, Resistor_SMD:R_1206_3216Metric_Pad1.30x1.75mm_HandSolder, F.Cu at (-38.0, 38.4)
- added R524: 2K, Resistor_SMD:R_1206_3216Metric_Pad1.30x1.75mm_HandSolder, F.Cu at (-38.0, 41.7)
- added R525: 2K43, Resistor_SMD:R_1206_3216Metric_Pad1.30x1.75mm_HandSolder, F.Cu at (-38.0, 45.0)
- added R526: 1K62, Resistor_SMD:R_1206_3216Metric_Pad1.30x1.75mm_HandSolder, F.Cu at (-38.0, 48.3)
- added R527: 1K, Resistor_SMD:R_1206_3216Metric_Pad1.30x1.75mm_HandSolder, F.Cu at (-32.0, 25.1)
- added R528: 5K62, Resistor_SMD:R_1206_3216Metric_Pad1.30x1.75mm_HandSolder, F.Cu at (-32.0, 28.4)
- added R529: 7K5, Resistor_SMD:R_1206_3216Metric_Pad1.30x1.75mm_HandSolder, F.Cu at (-32.0, 31.7)
- added R530: 2K21, Resistor_SMD:R_1206_3216Metric_Pad1.30x1.75mm_HandSolder, F.Cu at (-32.0, 35.1)
- added R531: 2K21, Resistor_SMD:R_1206_3216Metric_Pad1.30x1.75mm_HandSolder, F.Cu at (-32.0, 38.4)
- added R532: 3K92, Resistor_SMD:R_1206_3216Metric_Pad1.30x1.75mm_HandSolder, F.Cu at (-32.0, 41.7)
- added R533: 3K92, Resistor_SMD:R_1206_3216Metric_Pad1.30x1.75mm_HandSolder, F.Cu at (-32.0, 45.0)
- added R534: 10K, Resistor_SMD:R_1206_3216Metric_Pad1.30x1.75mm_HandSolder, F.Cu at (-32.0, 48.3)
- added R535: 10K, Resistor_SMD:R_1206_3216Metric_Pad1.30x1.75mm_HandSolder, F.Cu at (-26.1, 25.1)
- added R536: 47K5, Resistor_SMD:R_1206_3216Metric_Pad1.30x1.75mm_HandSolder, F.Cu at (-26.1, 28.4)
- added R537: 562, Resistor_SMD:R_1206_3216Metric_Pad1.30x1.75mm_HandSolder, F.Cu at (-26.1, 31.7)
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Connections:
- net /Connections/LDFREQ renamed /LDFREQ
- net /Connections/LOW_DIST renamed /LOW_DIST
- net /Integrator 1 & Loop Inverter//WR renamed /Integrator 1 & Loop Inverter/~{WR}
- net WR renamed /Integrator 1 & Loop Inverter/WR
- D21 pad 1: /Output IMD Attenuator/WR -> /WR
- D21 pad 10: /Output IMD Attenuator/SDI -> /SD1
- D21 pad 15: /Output IMD Attenuator/ENABLE -> /ENABLE
- D21 pad 3: /Output IMD Attenuator/CLK -> /CLK
- D22 pad 10: Net-(D22-~{CLR}) -> Net-(D22-~{STB3})
- D22 pad 13: Net-(D22-~{CLR}) -> unconnected-(D22-~{CLR}-Pad13)
- D22 pad 7: /Output IMD Attenuator/SD2 -> /Integrator 1 & Loop Inverter/SD2
- D22 pad 8: /Output IMD Attenuator/CLK -> /CLK
- D22 pad 9: /Output IMD Attenuator/~{WR} -> /~{WR}
- D30 pad 15: /Integrator 1 & Loop Inverter/SIN -> SIN
- D30 pad 7: /Integrator 1 & Loop Inverter/SD1 -> /SD1
- D30 pad 8: CLK -> /CLK
- D31 pad 3: CLK -> /CLK
- D31 pad 5: Net-(D30-SRO) -> Net-(D31-QP1)
- D32 pad 15: /Integrator 1 & Loop Inverter/COS -> /COS
- D32 pad 8: CLK -> /CLK
- D40 pad 15: /Integrator 2/LOOP -> /LOOP
- D40 pad 7: /Integrator 2/SD1 -> /SD1
- D40 pad 8: /Integrator 2/CLK -> /CLK
- D40 pad 9: /Integrator 2//WR -> /~{WR}
- D41 pad 1: /Integrator 2/WR -> /WR
- D41 pad 3: /Integrator 2/CLK -> /CLK
- N32 pad 6: /Integrator 1 & Loop Inverter/COS -> /COS
- N42 pad 6: /Integrator 2/SIN -> SIN
- V314 pad 3: /Integrator 1 & Loop Inverter/COS -> /COS
- X1 pad 10: /Connections/~{RD} -> /~{RD}
- X1 pad 11: /Connections/SDI -> /SDI
- X1 pad 12: /Connections/CLK -> /CLK
- X1 pad 7: /Connections/ENABLE -> /ENABLE
- X1 pad 8: /Connections/SDO -> /SDO
- X1 pad 9: /Connections/~{WR} -> /~{WR}
- X2 pad 1: /Output IMD Attenuator/COS -> /COS
- X50 pad 1: /Level Control (ALC)/COS -> /COS

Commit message: First round of autoplacement.
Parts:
- removed the D21 at (-83.3, 154.1)
- removed the D22 at (-46.9, 152.5)
- C206, C207, C211, C212, C215, C216, C300, C301, C305, C306, C307, C309, C310, C311, C312, C313, C314, C316, C317, C319, C320, C321, C400, C401, C405, C407, C409, C410, C415, C501, C502, C503, C505, C506, C507, C509, C510, C515, C516, C517, C520, C521, C522, D20, D21, D22, D23, D30, D31, D32, D40, D41, D50, N31, N33, N41, N50, N51, N52, N53, N54, N56, R200, R201, R202, R203, R204, R205, R207, R208, R209, R210, R211, R212, R215, R301, R305, R307, R309, R310, R311, R312, R313, R314, R315, R316, R317, R318, R319, R320, R321, R322, R323, R324, R325, R327, R328, R329, R330, R331, R332, R333, R334, R336, R337, R338, R341, R342, R343, R345, R346, R347, R405, R407, R409, R410, R411, R412, R413, R414, R415, R416, R417, R418, R419, R420, R421, R422, R423, R424, R425, R426, R427, R428, R429, R430, R500, R501, R503, R504, R506, R507, R508, R509, R510, R511, R512, R513, R514, R515, R516, R517, R518, R520, R521, R522, R523, R524, R525, R526, R527, R528, R529, R530, R531, R532, R533, R534, R536, R537, R539, R540, R542, V20, V21, V300, V301, V302, V303, V305, V306, V307, V311, V312, V313, V314, V316, V400, V402, V405, V406, V407, V501, V502, V503, V505, V506, V508, V509, V511, V513, V514, V537: moved to B.Cu
- moved V313 295.0 mm to (140.2, 45.9)
- moved V312 287.8 mm to (139.2, 58.9)
- moved V314 282.9 mm to (122.2, 39.9)
- moved V316 282.5 mm to (117.2, 39.9)
- moved C402 280.1 mm to (157.2, 46.9), turned to 180 degrees
- moved C410 278.3 mm to (159.2, 99.9)
- moved V311 277.9 mm to (134.2, 70.9)
- moved R420 274.7 mm to (170.2, 141.9), turned to 90 degrees
- moved R416 274.4 mm to (166.2, 74.9)
- moved R421 273.9 mm to (169.2, 50.9)
- moved R409 273.7 mm to (161.2, 99.9)
- moved R426 272.6 mm to (167.2, 63.9)
- moved R422 272.0 mm to (165.2, 43.9)
- moved R411 271.7 mm to (159.2, 116.9)
- moved R425 271.3 mm to (168.2, 74.9)
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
